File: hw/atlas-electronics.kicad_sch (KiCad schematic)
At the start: 0 parts

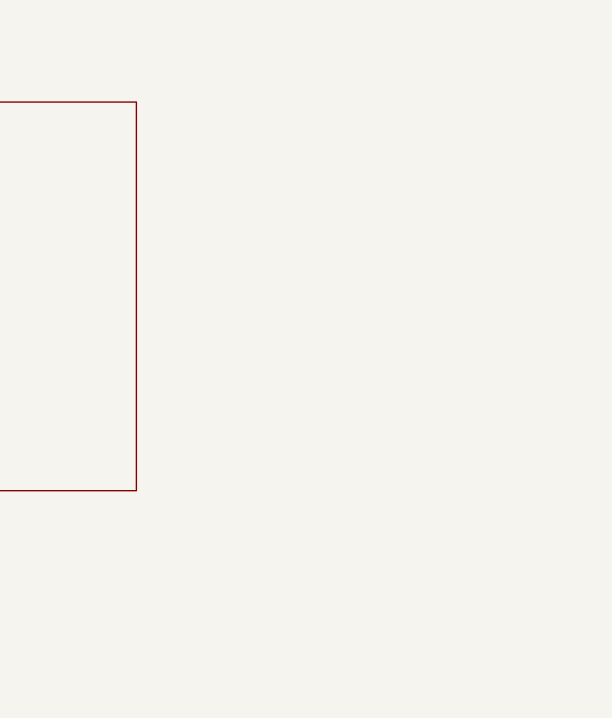
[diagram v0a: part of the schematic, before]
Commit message: add inverter-stage
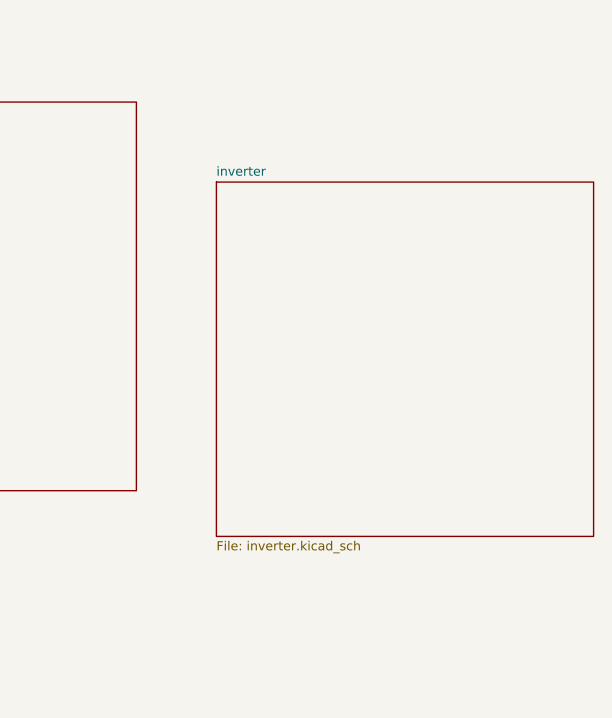
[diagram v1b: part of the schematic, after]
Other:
- added sheet inverter (inverter.kicad_sch)
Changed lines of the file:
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@@
 (kicad_sch
-	(version 20260306)
+	(version 20260826)
 	(generator "eeschema")
-	(generator_version "10.0")
+	(generator_version "10.99")
 	(paper "A4")
 	(bus
@@
 				)
 			)
+		)
+	)
+	(sheet
+		(at 177.8 74.93)
+		(size 41.91 39.37)
+		(exclude_from_sim no)
+		(in_bom yes)
+		(on_board yes)
+		(dnp no)
+		(fields_autoplaced yes)
+		(stroke
+			(width 0.1524)
+			(type solid)
+		)
+		(fill
+			(color 0 0 0 0)
+		)
+		(property "Sheetname" "inverter"
+			(at 177.8 74.3454 0)
+			(show_name no)
+			(do_not_autoplace no)
+			(effects
+				(font
+					(size 1.016 1.016)
+				)
+				(justify left bottom)
+			)
+		)
+		(property "Sheetfile" "inverter.kicad_sch"
+			(at 177.8 114.783 0)
+			(show_name no)
+			(do_not_autoplace no)
+			(effects
+				(font
+					(size 1.016 1.016)
+				)
+				(justify left top)
+			)
+		)
+		(instances
+			(project "atlas-electronics"
+				(path "/915bc1ff-7be5-4368-a2db-c4889af73afd"
+					(page "5")
+				)
+			)

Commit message: basic *.kicad_sch done
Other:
- sheet gate-driver renamed [3] - GATE-DRIVER
- sheet inverter renamed [4] - INVERTER
- sheet mcu renamed [1] - MCU
- sheet mcu-power renamed [2] - MCU POWER
- added sheet [10] - FDCAN Transceiver (fdcan.kicad_sch)
- added sheet [11] - Power Connects (power_conn.kicad_sch)
- added sheet [12] - STATUS LED (status-led.kicad_sch)
- added sheet [13] - MISC (misc.kicad_sch)
- added sheet [5] - SENSE VBAT (sense_temp.kicad_sch)
- added sheet [6] - SENSE TEMP (sense_vbat.kicad_sch)
- added sheet [7] - SENSE POS. (sense_pos.kicad_sch)
- added sheet [8] - Interconnects (interconnects.kicad_sch)
- sheet [1] - MCU ports: added DRV_EN, DRV_nF, EXT_HOMING_INT, SENSE_VBAT, SPI_ENC_CS_EXT, SPI_ENC_CS_ONB, STATUS_LED, {AUX1}, {AUX2}, {CRYSTAL}, {FDCAN}, {SENSE_TEMP}, {SPI_ENC}, {SWD}, {UID}; removed none
- sheet [3] - GATE-DRIVER ports: added DRV_EN, DRV_nF, GHA, GHB, GHC, GLA, GLB, GLC, SHA, SHB, SHC, SNA, SNB, SNC, SPA, SPB, SPC; removed none
- sheet [4] - INVERTER ports: added GHA, GHB, GHC, GLA, GLB, GLC, SHA, SHB, SHC, SNA, SNB, SNC, SPA, SPB, SPC; removed none

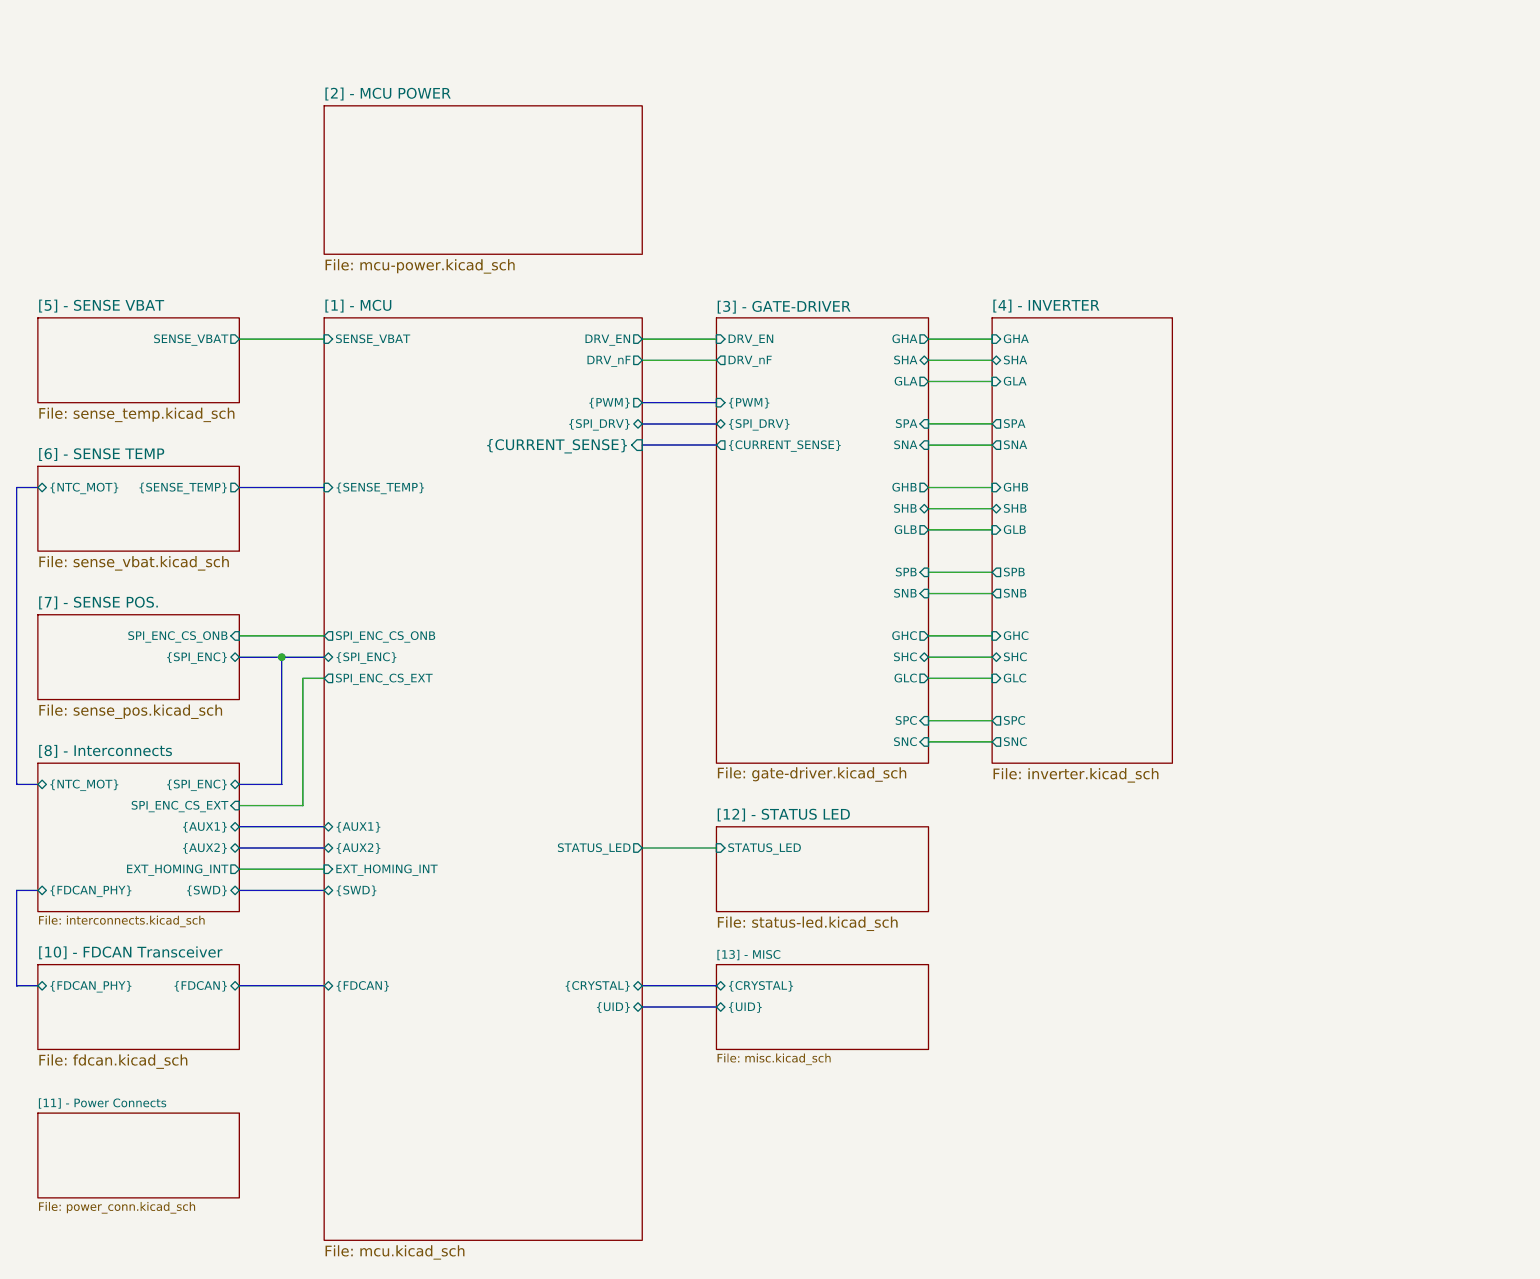
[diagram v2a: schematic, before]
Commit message: cleaned up *.kicad_sch
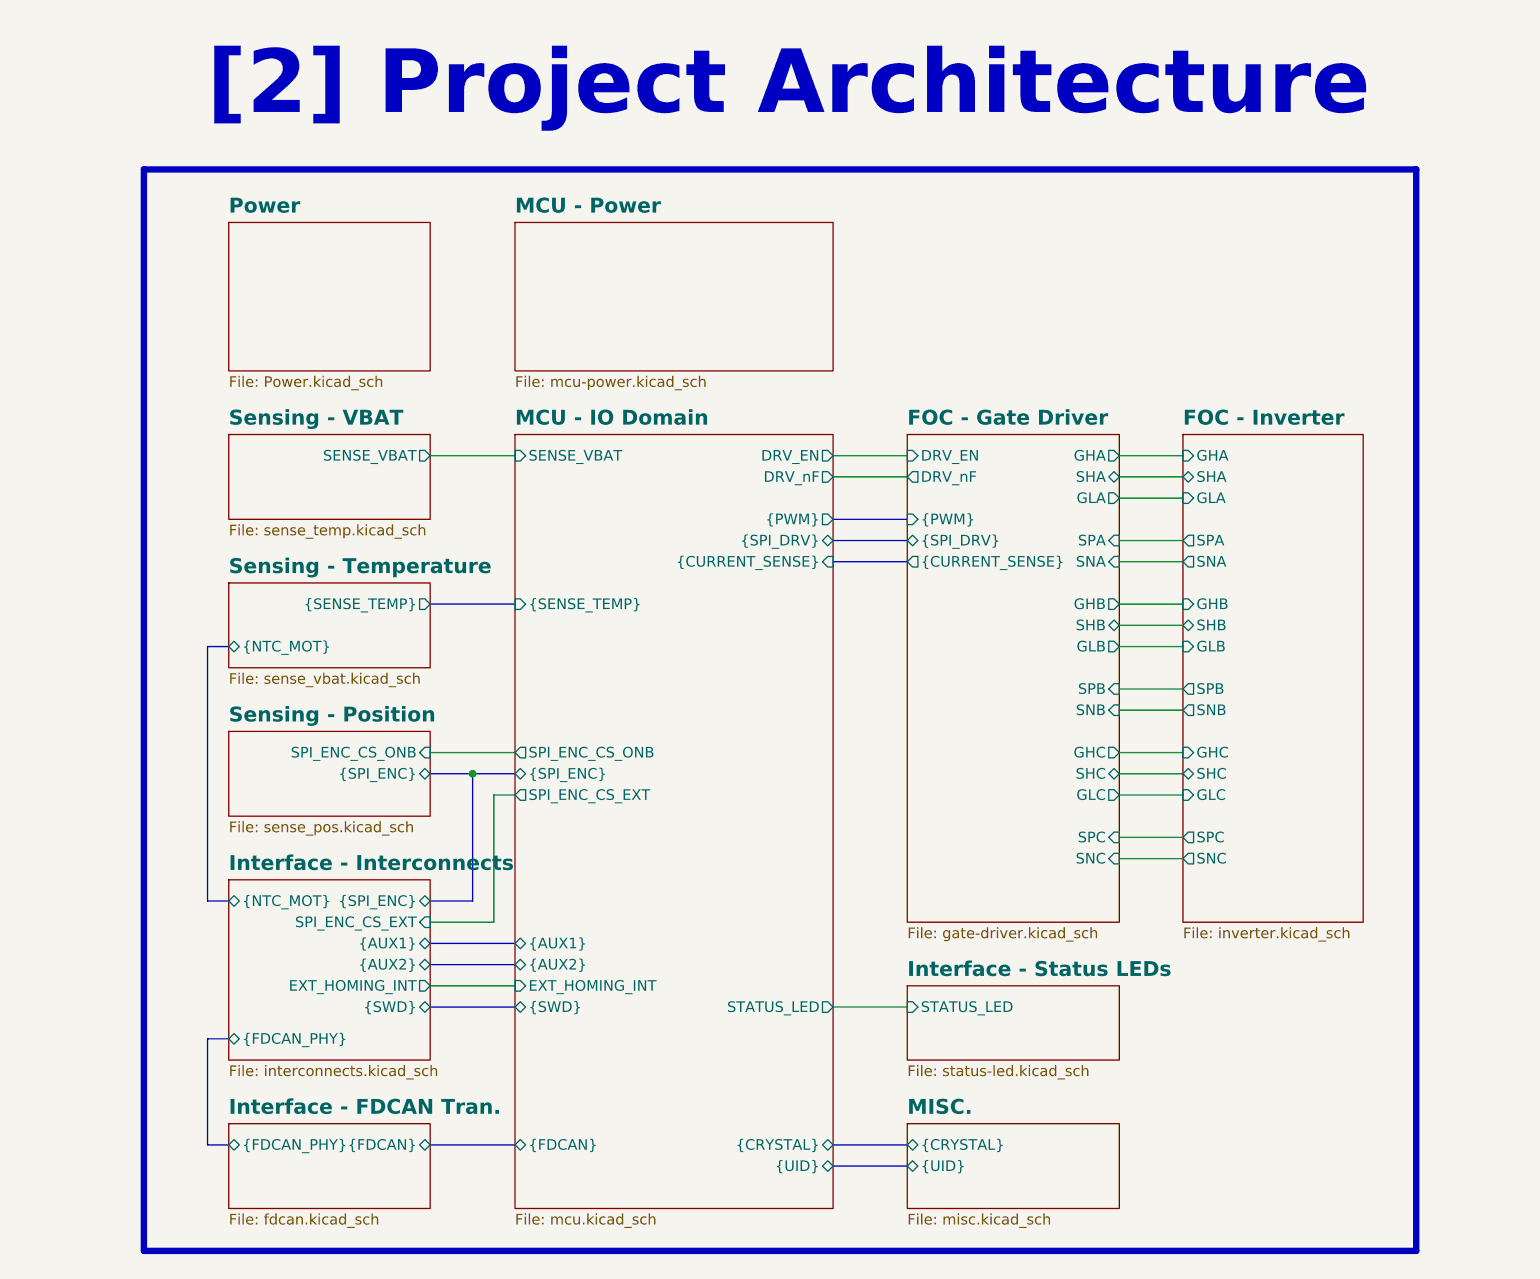
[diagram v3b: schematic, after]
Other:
- sheet [10] - FDCAN Transceiver renamed Interface - FDCAN Tran.
- sheet [12] - STATUS LED renamed Interface - Status LEDs
- sheet [13] - MISC renamed MISC.
- sheet [1] - MCU renamed MCU - IO Domain
- sheet [2] - MCU POWER renamed MCU - Power
- sheet [3] - GATE-DRIVER renamed FOC - Gate Driver
- sheet [4] - INVERTER renamed FOC - Inverter
- sheet [5] - SENSE VBAT renamed Sensing - VBAT
- sheet [6] - SENSE TEMP renamed Sensing - Temperature
- sheet [7] - SENSE POS. renamed Sensing - Position
- sheet [8] - Interconnects renamed Interface - Interconnects
- removed sheet [11] - Power Connects
- added sheet Power (Power.kicad_sch)
- note added: "[2] Project Architecture"
- title: (none) -> Project Architecture
